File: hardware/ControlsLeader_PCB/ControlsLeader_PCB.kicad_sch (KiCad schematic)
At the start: 13 parts, among them J1 CarCANConnector_Out, J2 PeripheralCAN_out, J3 CarCANConnector_In, J4 PeripheralCAN_in, J6 Conn_2Rows-09Pins, J7 Dash_LSOM_PWR, J8 Conn_2Rows-09Pins, U2 LeaderSOM

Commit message: Ready for final review
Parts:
- removed TP1: TestPoint, TestPoint:TestPoint_Pad_1.0x1.0mm, symbol Connector:TestPoint
- added F1: Fuse, Fuse:Fuseholder_Blade_Mini_Keystone_3568, symbol Device:Fuse
- added J15: Conn_01x04, Connector_Molex:Molex_Nano-Fit_105313-xx04_1x04_P2.50mm_Horizontal, symbol Connector_Generic:Conn_01x04
- added J16: SteeringConn_01x05, Connector_Molex:Molex_Nano-Fit_105313-xx05_1x05_P2.50mm_Horizontal, symbol Connector_Generic:Conn_01x05
- J6: value Conn_2Rows-09Pins -> DashConn1_2Rows-09Pins
- J8: value Conn_2Rows-09Pins -> DashConn2_2Rows-09Pins
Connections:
- net 3.3V_LDO: now also J6.3 (Pin_3), J6.5 (Pin_5), J6.7 (Pin_7), J8.1 (Pin_1), J8.3 (Pin_3), J8.5 (Pin_5), J8.7 (Pin_7), F1.2, J15.1 (Pin_1), J16.1 (Pin_1)
- net Cruise_Enable_GPIO_IN: now also J8.4 (Pin_4); no longer J6.8 (Pin_8)
- net Cruise_Set_GPIO_IN: now also J8.2 (Pin_2); no longer J6.7 (Pin_7)
- net Extra_LED6: no longer U2.31 (ADC1_IN12)
- net Fwd_SW_GPIO: now also J6.4 (Pin_4); no longer J6.5 (Pin_5)
- net GND: no longer J8.8 (Pin_8)
- net Hazard_GPIO_IN: now also J8.8 (Pin_8); no longer J8.1 (Pin_1)
- net Horn_24V_Signal_Out: no longer J8.3 (Pin_3)
- net Horn_GPIO_IN: now also J16.4 (Pin_4); no longer J8.7 (Pin_7)
- net Ign_OFF_GPIO: now also J15.3 (Pin_3); no longer J6.6 (Pin_6)
- net Ign_arr_GPIO: now also J15.4 (Pin_4); no longer J6.4 (Pin_4)
- net Ign_mtr_GPIO: now also J15.2 (Pin_2); no longer J6.2 (Pin_2)
- net Left_Blinker_ON: now also J16.2 (Pin_2); no longer J8.6 (Pin_6)
- net Neutral_Gear_GPIO: now also J6.6 (Pin_6); no longer J8.2 (Pin_2)
- net Regen_Enable_GPIO_IN: now also J8.6 (Pin_6); no longer J8.5 (Pin_5)
- net Rev_SW_GPIO: now also J6.2 (Pin_2); no longer J6.3 (Pin_3)
- net Right_Blinker_ON: now also J16.3 (Pin_3); no longer J8.4 (Pin_4)
- new net 5v_3.3v_LDO/3.3V_LDO: F1.1
- new net Regen_Active_GPIO_IN: J16.5 (Pin_5), U2.31 (ADC1_IN12)
- no-connect marks 8 -> 5
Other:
- removed sheet NMOS Level Shifter
- sheet Steering_Wheel ports: added Regen_Active_GPIO_IN; removed none
- note added: "LSOM + Dash PWR"
- note added: "Steering Connector"
- note removed: "Controls Leader + Dash PWR"

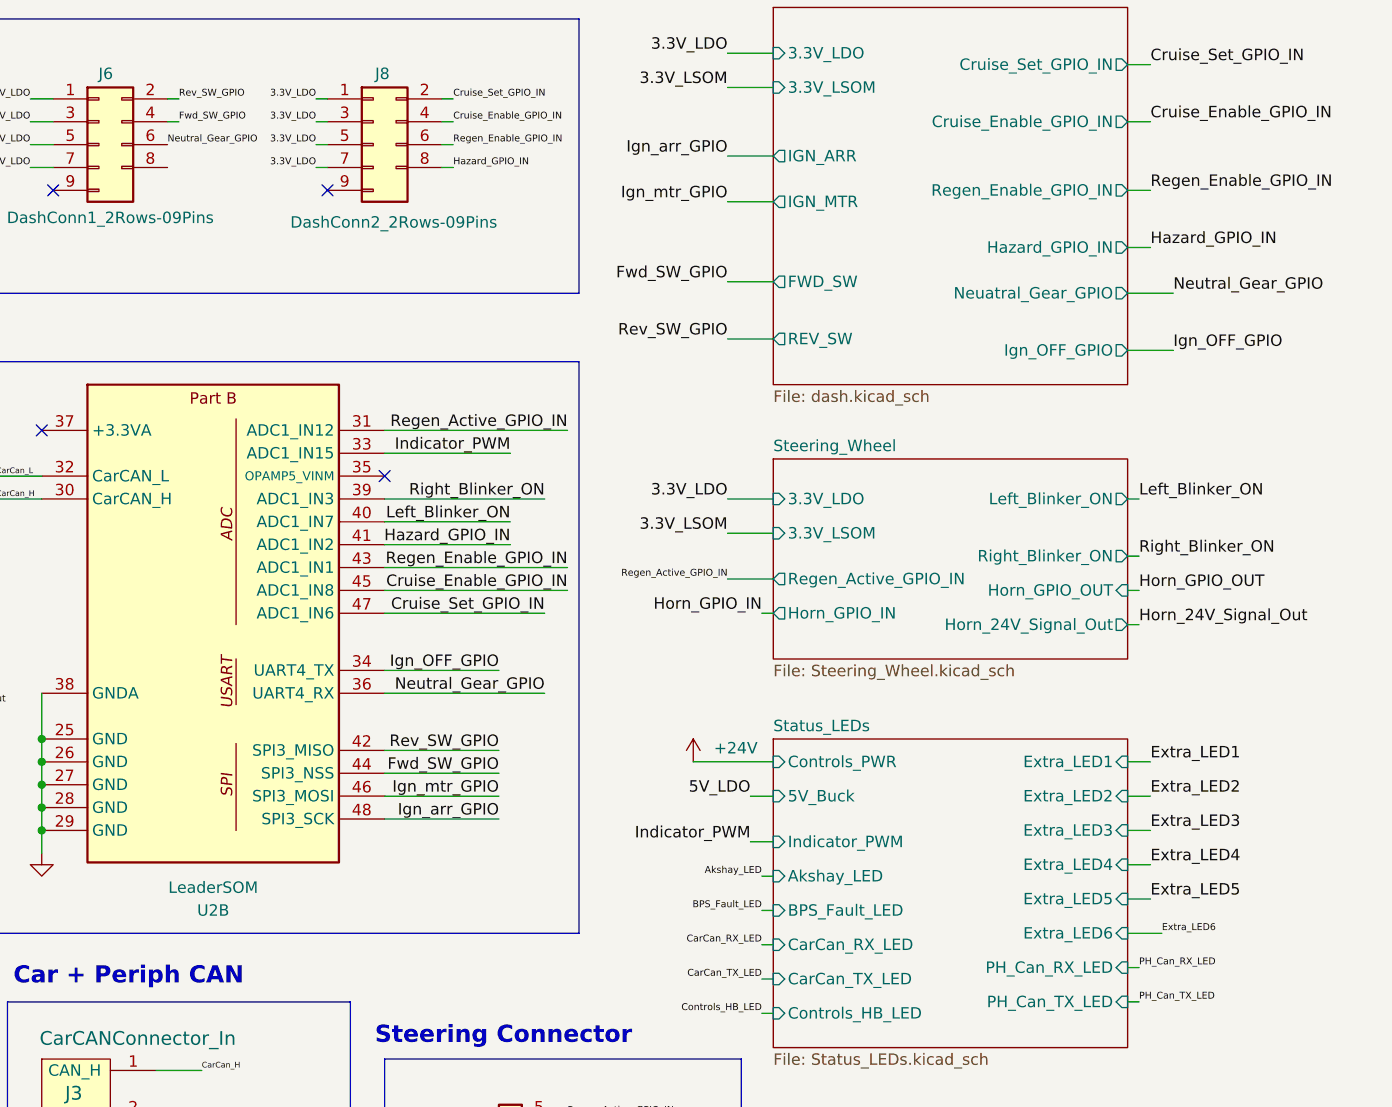
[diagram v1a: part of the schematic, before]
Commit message: Removed Extra LED 6
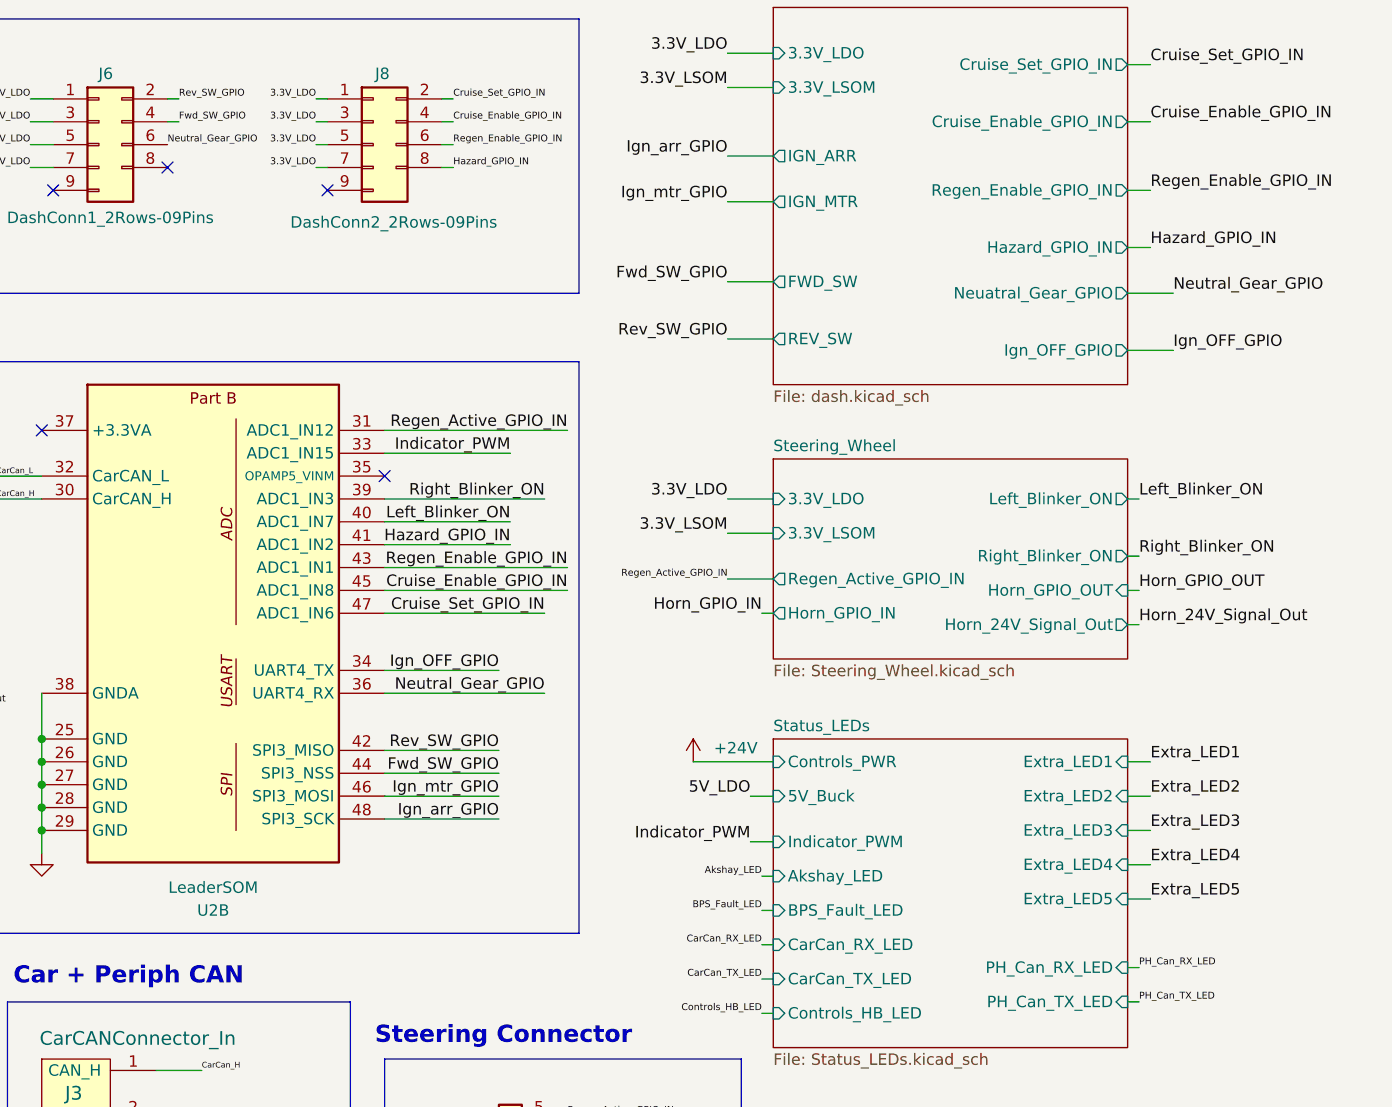
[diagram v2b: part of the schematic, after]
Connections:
- no-connect marks 5 -> 6
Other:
- sheet Status_LEDs ports: added none; removed Extra_LED6
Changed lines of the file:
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@@
 	)
 	(no_connect
+		(at 152.4 39.37)
+	)
+	(no_connect
 		(at 176.53 73.66)
 	)
@@
 	(wire
 		(pts
-			(xy 259.08 124.46) (xy 262.89 124.46)
-		)
-		(stroke
-			(width 0)
-			(type default)
-		)
-	)
-	(wire
-		(pts
 			(xy 219.71 114.3) (xy 217.17 114.3)
 		)
@@
 		)
 	)
-	(label "Extra_LED6"
-		(at 262.89 124.46 0)
-		(effects
-			(font
-				(size 0.762 0.762)
-			)
-			(justify left bottom)
-		)
-	)
 	(label "Horn_24V_Signal_Out"
 		(at 260.35 90.17 0)
@@
 			)
 		)
-		(pin "Extra_LED6" input
-			(at 259.08 124.46 0)
-			(effects
-				(font
-					(size 1.27 1.27)
-				)
-				(justify right)
-			)
-		)

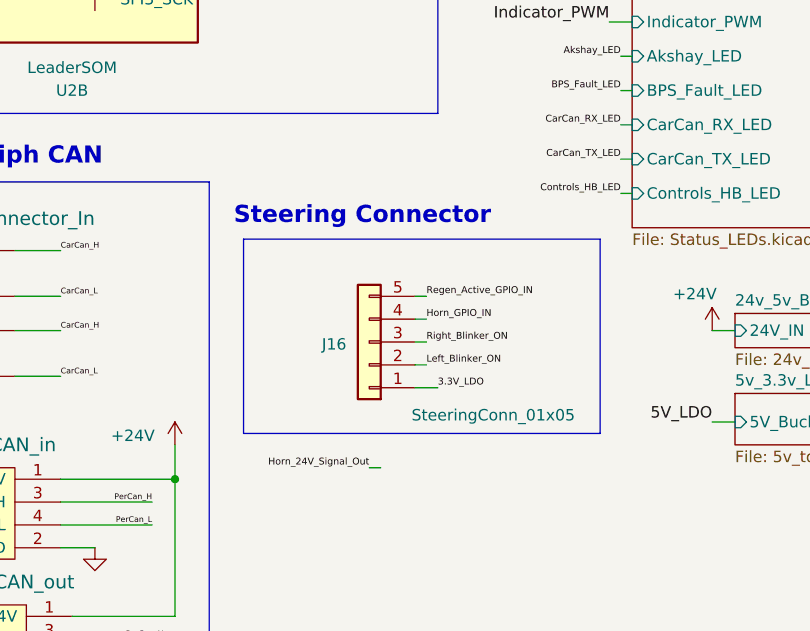
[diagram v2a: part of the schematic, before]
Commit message: Updated LSOM status LED and horn 24v signal connector layout
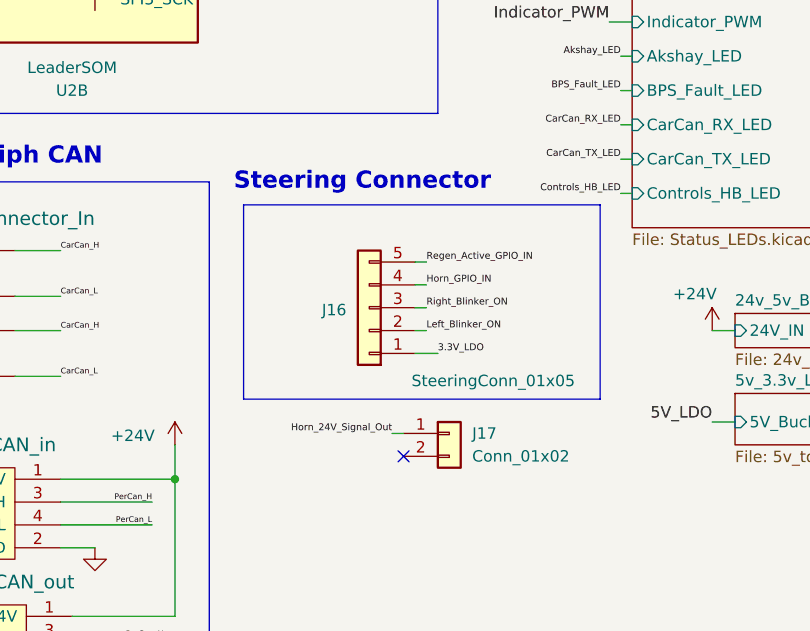
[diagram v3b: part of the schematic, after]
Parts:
- added J17: Conn_01x02, symbol Connector_Generic:Conn_01x02
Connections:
- net Horn_24V_Signal_Out: now also J17.1 (Pin_1)
- no-connect marks 6 -> 7
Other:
- moved on the sheet: J16
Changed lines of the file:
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@@
 	(paper "A4")
 	(rectangle
-		(start 176.53 138.43)
-		(end 216.154 160.02)
+		(start 176.53 134.62)
+		(end 216.154 156.21)
 		(stroke
 			(width 0)
@@
 	(text "Steering Connector"
 		(exclude_from_sim no)
-		(at 189.738 135.89 0)
+		(at 189.738 132.08 0)
 		(effects
 			(font
@@
 	)
 	(no_connect
+		(at 194.31 162.56)
+	)
+	(no_connect
 		(at 139.7 41.91)
 	)
@@
 	(wire
 		(pts
-			(xy 196.85 152.4) (xy 195.58 152.4)
+			(xy 196.85 148.59) (xy 195.58 148.59)
 		)
 		(stroke
@@
 	(wire
 		(pts
-			(xy 198.12 154.94) (xy 195.58 154.94)
+			(xy 198.12 151.13) (xy 195.58 151.13)
 		)
 		(stroke
@@
 	(wire
 		(pts
-			(xy 196.85 149.86) (xy 195.58 149.86)
+			(xy 196.85 146.05) (xy 195.58 146.05)
 		)
 		(stroke
@@
 	(wire
 		(pts
-			(xy 196.85 147.32) (xy 195.58 147.32)
+			(xy 196.85 143.51) (xy 195.58 143.51)
 		)
 		(stroke
@@
 	(wire
 		(pts
-			(xy 195.58 144.78) (xy 196.85 144.78)
+			(xy 195.58 140.97) (xy 196.85 140.97)
 		)
 		(stroke
@@
 	(wire
 		(pts
-			(xy 190.5 163.83) (xy 191.77 163.83)
+			(xy 193.04 160.02) (xy 194.31 160.02)
 		)
 		(stroke
@@
 	)
 	(label "3.3V_LDO"
-		(at 198.12 154.94 0)
+		(at 198.12 151.13 0)
 		(effects
 			(font
@@
 	)
 	(label "Right_Blinker_ON"
-		(at 196.85 149.86 0)
+		(at 196.85 146.05 0)
 		(effects
 			(font
@@
 	)
 	(label "Horn_GPIO_IN"
-		(at 196.85 147.32 0)
+		(at 196.85 143.51 0)
 		(effects
 			(font
@@
 	)
 	(label "Regen_Active_GPIO_IN"
-		(at 196.85 144.78 0)
+		(at 196.85 140.97 0)
 		(effects
 			(font
@@
 	)
 	(label "Left_Blinker_ON"
-		(at 196.85 152.4 0)
+		(at 196.85 148.59 0)
 		(effects
 			(font
@@
 	)
 	(label "Horn_24V_Signal_Out"
-		(at 190.5 163.83 180)
+		(at 193.04 160.02 180)
 		(effects
 			(font
@@
 	)
 	(symbol
+		(lib_id "Connector_Generic:Conn_01x02")
+		(at 199.39 160.02 0)
+		(unit 1)
+		(exclude_from_sim no)
+		(in_bom yes)
+		(on_board yes)
+		(dnp no)
+		(fields_autoplaced yes)
+		(property "Reference" "J17"
+			(at 201.93 160.0199 0)
+			(effects
+				(font
+					(size 1.27 1.27)
+				)
+				(justify left)
+			)
+		)
+		(property "Value" "Conn_01x02"
+			(at 201.93 162.5599 0)
+			(effects
+				(font
+					(size 1.27 1.27)
+				)
+				(justify left)
+			)
+		)
+		(property "Footprint" ""
+			(at 199.39 160.02 0)
+			(effects
+				(font
+					(size 1.27 1.27)
+				)
+				(hide yes)
+			)
+		)
+		(property "Datasheet" "~"
+			(at 199.39 160.02 0)
+			(effects
+				(font
+					(size 1.27 1.27)
+				)
+				(hide yes)
+			)
+		)
+		(property "Description" "Generic connector, single row, 01x02, script generated (kicad-library-utils/schlib/autogen/connector/)"
+			(at 199.39 160.02 0)
+			(effects
+				(font
+					(size 1.27 1.27)
+				)
+				(hide yes)
+			)
+		)
+		(pin "1"
+		)
+		(pin "2"
+		)
+		(instances
+			(project ""
+				(path "/298dad81-302c-41c7-874b-fcde1c3cde17"
+					(reference "J17")
+					(unit 1)
+				)
+			)
+		)
+	)
+	(symbol
 		(lib_id "power:+24V")
 		(at 168.91 161.29 0)
@@
 	(symbol
 		(lib_id "Connector_Generic:Conn_01x05")
-		(at 190.5 149.86 180)
+		(at 190.5 146.05 180)
 		(unit 1)
 		(exclude_from_sim no)
@@
 		(dnp no)
 		(property "Reference" "J16"
-			(at 187.96 150.114 0)
+			(at 187.96 146.304 0)
 			(effects
 				(font
@@
 		)
 		(property "Value" "SteeringConn_01x05"
-			(at 213.36 157.988 0)
+			(at 213.36 154.178 0)
 			(effects
 				(font
@@
 		)
 		(property "Footprint" "Connector_Molex:Molex_Nano-Fit_105313-xx05_1x05_P2.50mm_Horizontal"
-			(at 190.5 149.86 0)
+			(at 190.5 146.05 0)
 			(effects
 				(font
@@
 		)
 		(property "Datasheet" "~"
-			(at 190.5 149.86 0)
+			(at 190.5 146.05 0)
 			(effects
 				(font
@@
 		)
 		(property "Description" "Generic connector, single row, 01x05, script generated (kicad-library-utils/schlib/autogen/connector/)"
-			(at 190.5 149.86 0)
+			(at 190.5 146.05 0)
 			(effects
 				(font

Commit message: All footprints added
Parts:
- J17: footprint (none) -> Connector_Molex:Molex_Nano-Fit_105313-xx02_1x02_P2.50mm_Horizontal
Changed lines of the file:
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@@
 			)
 		)
-		(property "Footprint" ""
+		(property "Footprint" "Connector_Molex:Molex_Nano-Fit_105313-xx02_1x02_P2.50mm_Horizontal"
 			(at 199.39 160.02 0)
 			(effects
